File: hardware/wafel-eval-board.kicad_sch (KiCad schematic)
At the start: 50 parts, among them J101 CAN PORT, J102 SW, Q101 AO3422, U101 LM5163DDA

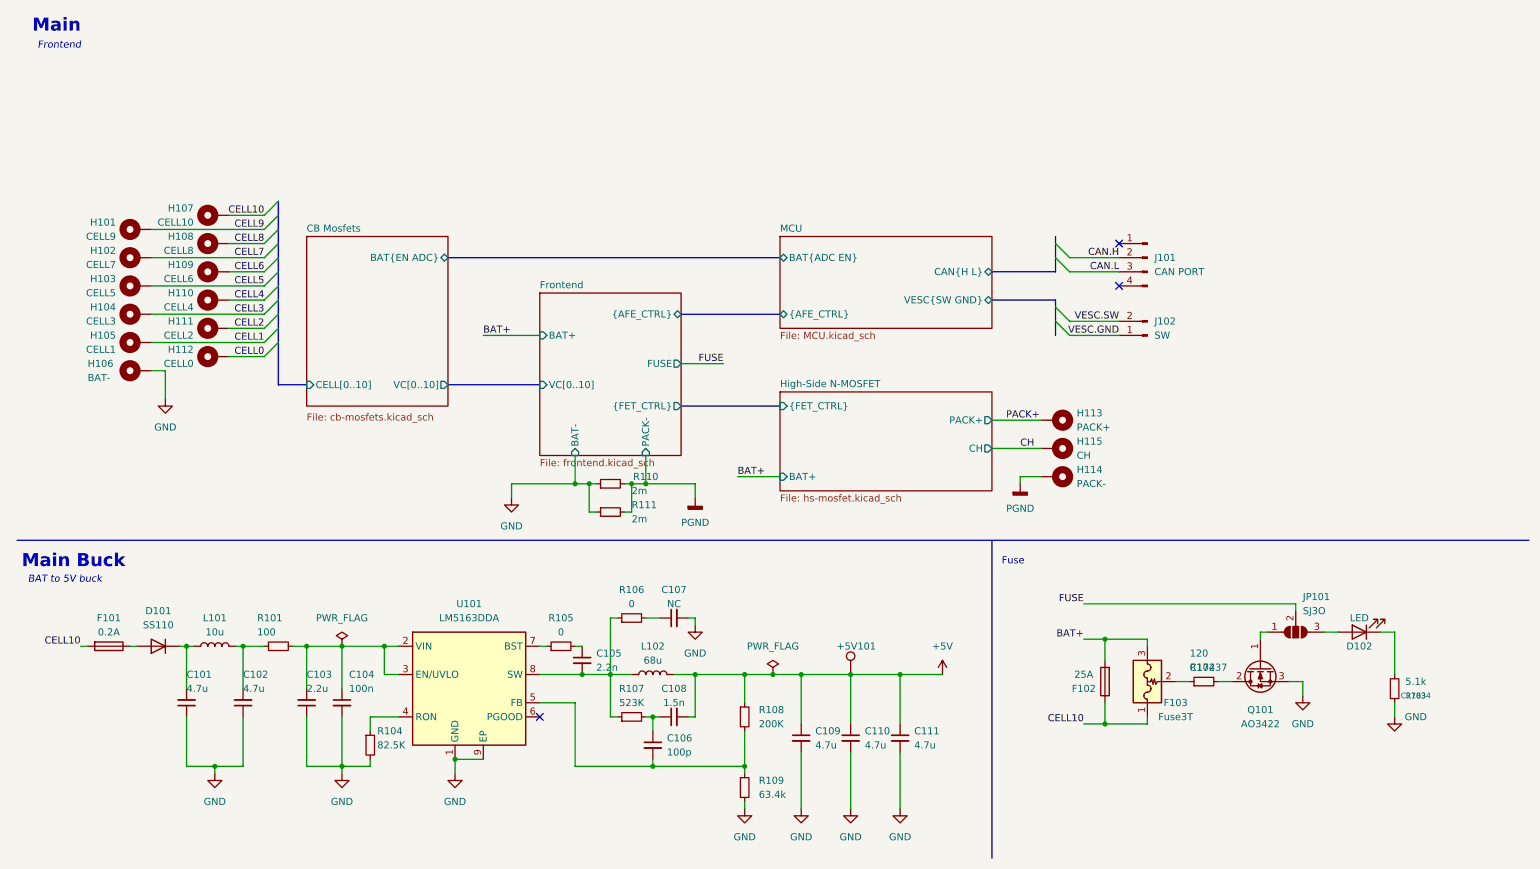
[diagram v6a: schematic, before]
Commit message: placed c mosfet
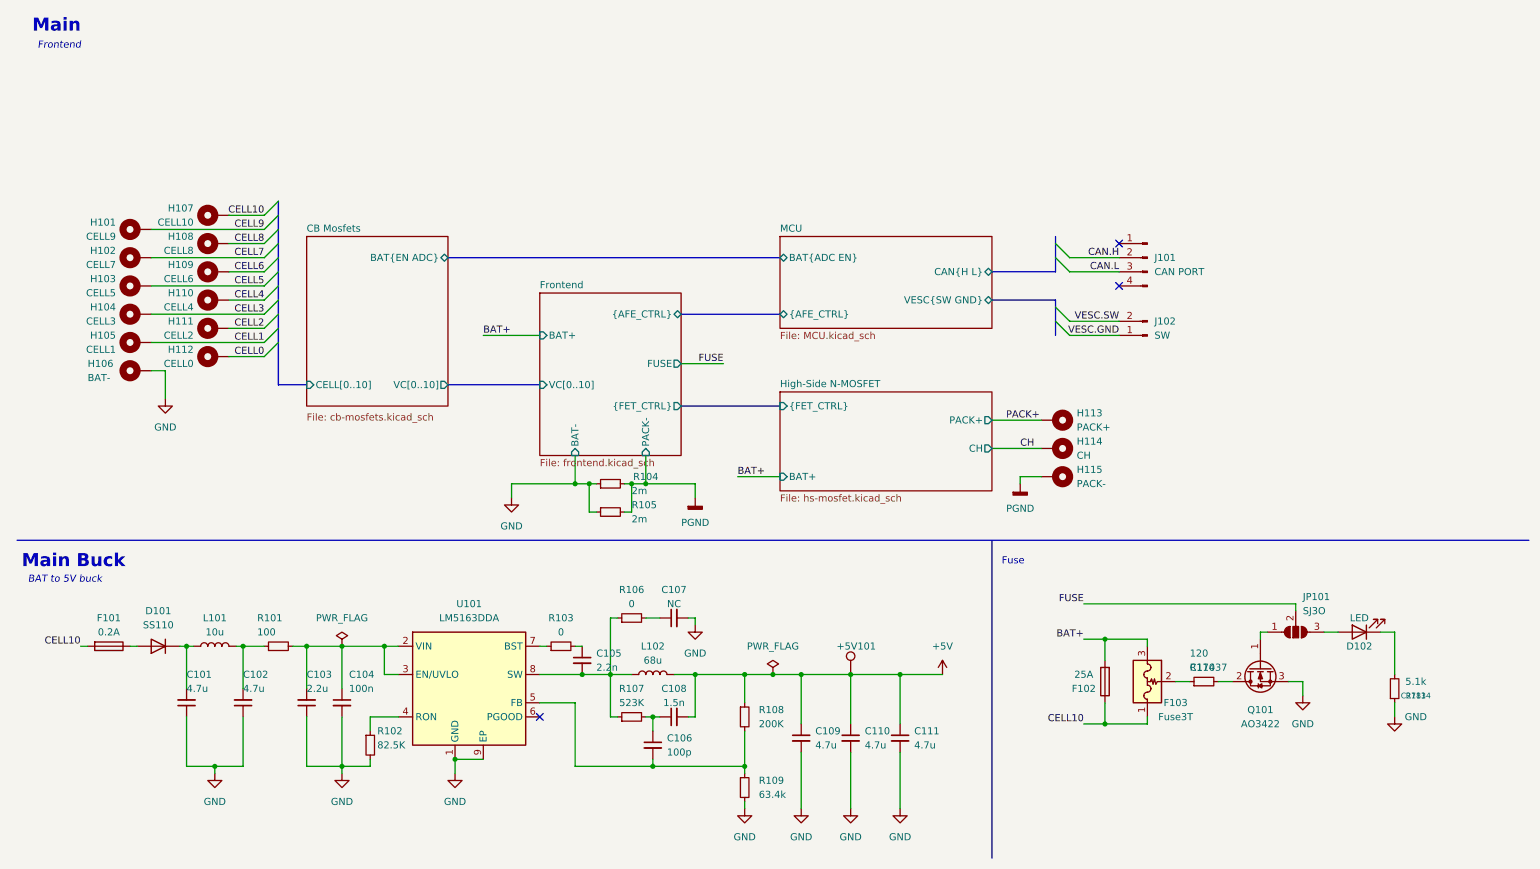
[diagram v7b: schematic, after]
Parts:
- C105, C106, C107, C108: footprint Capacitor_SMD:C_0805_2012Metric -> Capacitor_SMD:C_0603_1608Metric
- R101, R106, R107, R108, R109: footprint Resistor_SMD:R_0805_2012Metric -> Resistor_SMD:R_0603_1608Metric
- R102: renamed from R104; footprint Resistor_SMD:R_0805_2012Metric -> Resistor_SMD:R_0603_1608Metric
- R103: renamed from R105; footprint Resistor_SMD:R_0805_2012Metric -> Resistor_SMD:R_0603_1608Metric
- R104: renamed from R110; footprint Resistor_SMD:R_0805_2012Metric -> Resistor_SMD:R_0603_1608Metric
- R105: renamed from R111; footprint Resistor_SMD:R_0805_2012Metric -> Resistor_SMD:R_0603_1608Metric
- R110: renamed from R102; footprint Resistor_SMD:R_0805_2012Metric -> Resistor_SMD:R_0603_1608Metric
- R111: renamed from R103; footprint Resistor_SMD:R_0805_2012Metric -> Resistor_SMD:R_0603_1608Metric
- renumbered H115 to H114, H114 to H115
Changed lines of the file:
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@@
 		(in_pos_files yes)
 		(dnp no)
-		(property "Reference" "#PWR0105"
+		(property "Reference" "#PWR0115"
 			(at 260.35 147.32 0)
 			(hide yes)
@@
 			(project "wafel-eval-board"
 				(path "/3e668e3e-3e16-4665-a807-4735962c41d3"
-					(reference "#PWR0105")
+					(reference "#PWR0115")
 					(unit 1)
 				)
@@
 		(dnp no)
 		(fields_autoplaced yes)
-		(property "Reference" "#PWR0115"
+		(property "Reference" "#PWR0106"
 			(at 134.62 107.95 0)
 			(hide yes)
@@
 			(project "wafel-eval-board"
 				(path "/3e668e3e-3e16-4665-a807-4735962c41d3"
-					(reference "#PWR0115")
+					(reference "#PWR0106")
 					(unit 1)
 				)
@@
 		(dnp no)
 		(fields_autoplaced yes)
-		(property "Reference" "R105"
+		(property "Reference" "R103"
 			(at 110.49 123.19 90)
 			(show_name no)
@@
 			)
 		)
-		(property "Footprint" "Resistor_SMD:R_0805_2012Metric"
+		(property "Footprint" "Resistor_SMD:R_0603_1608Metric"
 			(at 110.49 128.27 0)
 			(hide yes)
@@
 			(project "wafel-eval-board"
 				(path "/3e668e3e-3e16-4665-a807-4735962c41d3"
-					(reference "R105")
+					(reference "R103")
 					(unit 1)
 				)
@@
 			)
 		)
-		(property "Footprint" "Capacitor_SMD:C_0805_2012Metric"
+		(property "Footprint" "Capacitor_SMD:C_0603_1608Metric"
 			(at 127 146.05 0)
 			(hide yes)
@@
 			)
 		)
-		(property "Footprint" "Resistor_SMD:R_0805_2012Metric"
+		(property "Footprint" "Resistor_SMD:R_0603_1608Metric"
 			(at 123.19 123.19 0)
 			(hide yes)
@@
 		(dnp no)
 		(fields_autoplaced yes)
-		(property "Reference" "#PWR0114"
+		(property "Reference" "#PWR0105"
 			(at 101.6 107.95 0)
 			(hide yes)
@@
 			(project "wafel-eval-board"
 				(path "/3e668e3e-3e16-4665-a807-4735962c41d3"
-					(reference "#PWR0114")
+					(reference "#PWR0105")
 					(unit 1)
 				)
@@
 			)
 		)
-		(property "Footprint" "Resistor_SMD:R_0805_2012Metric"
+		(property "Footprint" "Resistor_SMD:R_0603_1608Metric"
 			(at 143.51 140.97 0)
 			(hide yes)
@@
 			)
 		)
-		(property "Footprint" "Resistor_SMD:R_0805_2012Metric"
+		(property "Footprint" "Resistor_SMD:R_0603_1608Metric"
 			(at 123.19 140.97 0)
 			(hide yes)
@@
 		(dnp no)
 		(fields_autoplaced yes)
-		(property "Reference" "#FLG0102"
+		(property "Reference" "#FLG0101"
 			(at 71.12 126.365 0)
 			(hide yes)
@@
 			(project "wafel-eval-board"
 				(path "/3e668e3e-3e16-4665-a807-4735962c41d3"
-					(reference "#FLG0102")
+					(reference "#FLG0101")
 					(unit 1)
 				)
@@
 			)
 		)
-		(property "Footprint" "Resistor_SMD:R_0805_2012Metric"
+		(property "Footprint" "Resistor_SMD:R_0603_1608Metric"
 			(at 143.51 153.67 0)
 			(hide yes)
@@
 			)
 		)
-		(property "Footprint" "Capacitor_SMD:C_0805_2012Metric"
+		(property "Footprint" "Capacitor_SMD:C_0603_1608Metric"
 			(at 130.81 140.97 0)
 			(hide yes)
@@
 		(in_pos_files yes)
 		(dnp no)
-		(property "Reference" "R111"
+		(property "Reference" "R105"
 			(at 123.19 102.87 90)
 			(show_name no)
@@
 			)
 		)
-		(property "Footprint" "Resistor_SMD:R_0805_2012Metric"
+		(property "Footprint" "Resistor_SMD:R_0603_1608Metric"
 			(at 119.38 104.14 0)
 			(hide yes)
@@
 			(project "wafel-eval-board"
 				(path "/3e668e3e-3e16-4665-a807-4735962c41d3"
-					(reference "R111")
+					(reference "R105")
 					(unit 1)
 				)
@@
 		(dnp no)
 		(fields_autoplaced yes)
-		(property "Reference" "#PWR0104"
+		(property "Reference" "#PWR0103"
 			(at 71.12 157.48 0)
 			(hide yes)
@@
 			(project "wafel-eval-board"
 				(path "/3e668e3e-3e16-4665-a807-4735962c41d3"
-					(reference "#PWR0104")
+					(reference "#PWR0103")
 					(unit 1)
 				)
@@
 			)
 		)
-		(property "Footprint" "Capacitor_SMD:C_0805_2012Metric"
+		(property "Footprint" "Capacitor_SMD:C_0603_1608Metric"
 			(at 114.3 130.81 0)
 			(hide yes)
@@
 		(in_pos_files yes)
 		(dnp no)
-		(property "Reference" "R104"
+		(property "Reference" "R102"
 			(at 77.47 143.51 0)
 			(show_name no)
@@
 			)
 		)
-		(property "Footprint" "Resistor_SMD:R_0805_2012Metric"
+		(property "Footprint" "Resistor_SMD:R_0603_1608Metric"
 			(at 76.2 146.05 0)
 			(hide yes)
@@
 			(project "wafel-eval-board"
 				(path "/3e668e3e-3e16-4665-a807-4735962c41d3"
-					(reference "R104")
+					(reference "R102")
 					(unit 1)
 				)
@@
 		(in_pos_files yes)
 		(dnp no)
-		(property "Reference" "H114"
+		(property "Reference" "H115"
 			(at 203.2 96.5199 90)
 			(show_name no)
@@
 			(project "wafel-eval-board"
 				(path "/3e668e3e-3e16-4665-a807-4735962c41d3"
-					(reference "H114")
+					(reference "H115")
 					(unit 1)
 				)
@@
 			)
 		)
-		(property "Footprint" "Resistor_SMD:R_0805_2012Metric"
+		(property "Footprint" "Resistor_SMD:R_0603_1608Metric"
 			(at 59.69 128.27 0)
 			(hide yes)
@@
 		(in_pos_files yes)
 		(dnp no)
-		(property "Reference" "H115"
+		(property "Reference" "H114"
 			(at 203.2 91.4399 90)
 			(show_name no)
@@
 			(project "wafel-eval-board"
 				(path "/3e668e3e-3e16-4665-a807-4735962c41d3"
-					(reference "H115")
+					(reference "H114")
 					(unit 1)
 				)
@@
 		(in_pos_files yes)
 		(dnp no)
-		(property "Reference" "R110"
+		(property "Reference" "R104"
 			(at 125.73 97.79 90)
 			(show_name no)
@@
 			)
 		)
-		(property "Footprint" "Resistor_SMD:R_0805_2012Metric"
+		(property "Footprint" "Resistor_SMD:R_0603_1608Metric"
 			(at 119.38 99.06 0)
 			(hide yes)
@@
 			(project "wafel-eval-board"
 				(path "/3e668e3e-3e16-4665-a807-4735962c41d3"
-					(reference "R110")
+					(reference "R104")
 					(unit 1)
 				)
@@
 		(dnp no)
 		(fields_autoplaced yes)
-		(property "Reference" "#PWR0103"
+		(property "Reference" "#PWR0114"
 			(at 243.84 143.51 0)
 			(hide yes)
@@
 			(project "wafel-eval-board"
 				(path "/3e668e3e-3e16-4665-a807-4735962c41d3"
-					(reference "#PWR0103")
+					(reference "#PWR0114")
 					(unit 1)
 				)
@@
 		(in_pos_files yes)
 		(dnp no)
-		(property "Reference" "R103"
+		(property "Reference" "R111"
 			(at 264.16 137.16 0)
 			(show_name no)
@@
 			)
 		)
-		(property "Footprint" "Resistor_SMD:R_0805_2012Metric"
+		(property "Footprint" "Resistor_SMD:R_0603_1608Metric"
 			(at 260.35 135.89 0)
 			(hide yes)
@@
 			(project "wafel-eval-board"
 				(path "/3e668e3e-3e16-4665-a807-4735962c41d3"
-					(reference "R103")
+					(reference "R111")
 					(unit 1)
 				)
@@
 		(dnp no)
 		(fields_autoplaced yes)
-		(property "Reference" "#FLG0101"
+		(property "Reference" "#FLG0102"
 			(at 148.59 131.445 0)
 			(hide yes)
@@
 			(project "wafel-eval-board"
 				(path "/3e668e3e-3e16-4665-a807-4735962c41d3"
-					(reference "#FLG0101")
+					(reference "#FLG0102")
 					(unit 1)
 				)
@@
 			)
 		)
-		(property "Footprint" "Capacitor_SMD:C_0805_2012Metric"
+		(property "Footprint" "Capacitor_SMD:C_0603_1608Metric"
 			(at 130.81 123.19 0)
 			(hide yes)
@@
 		(in_pos_files yes)
 		(dnp no)
-		(property "Reference" "R102"
+		(property "Reference" "R110"
 			(at 223.52 132.08 90)
 			(show_name no)
@@
 			)
 		)
-		(property "Footprint" "Resistor_SMD:R_0805_2012Metric"
+		(property "Footprint" "Resistor_SMD:R_0603_1608Metric"
 			(at 226.06 134.62 0)
 			(hide yes)
@@
 			(project "wafel-eval-board"
 				(path "/3e668e3e-3e16-4665-a807-4735962c41d3"
-					(reference "R102")
+					(reference "R110")
 					(unit 1)
 				)
@@
 		(dnp no)
 		(fields_autoplaced yes)
-		(property "Reference" "#PWR0106"
+		(property "Reference" "#PWR0104"
 			(at 91.44 157.48 0)
 			(hide yes)
@@
 			(project "wafel-eval-board"
 				(path "/3e668e3e-3e16-4665-a807-4735962c41d3"
-					(reference "#PWR0106")
+					(reference "#PWR0104")
 					(unit 1)
 				)

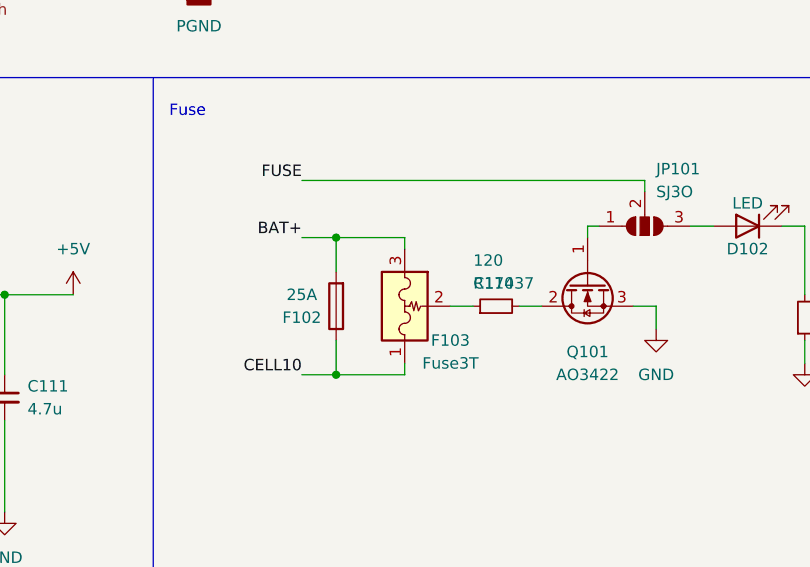
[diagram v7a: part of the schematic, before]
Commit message: placed c mosfet
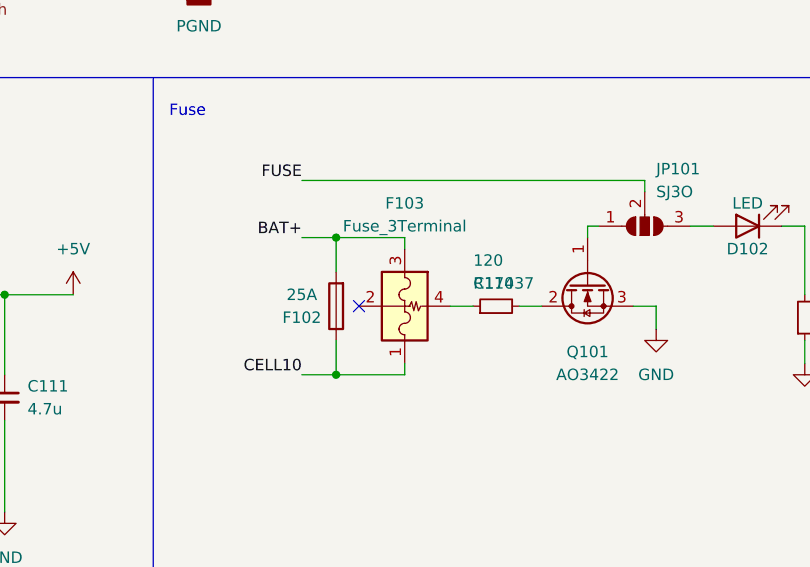
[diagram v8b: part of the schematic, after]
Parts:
- F103: value Fuse3T -> Fuse_3Terminal; footprint (none) -> wafel-eval-board:Fuse_SMD-3P_5.4x3.2mm
- JP101: footprint (none) -> Jumper:SolderJumper-3_P2.0mm_Open_TrianglePad1.0x1.5mm
- Q101: footprint (none) -> Package_TO_SOT_SMD:SOT-23
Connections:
- net at F103.2: no longer R110.1
- new net: F103.4, R110.1
- no-connect marks 3 -> 4
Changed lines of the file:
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@@
 	)
 	(no_connect
+		(at 210.82 134.62)
+	)
+	(no_connect
 		(at 210.82 63.5)
 	)
@@
 	)
 	(symbol
+		(lib_id "wafel-eval-board:Fuse_3Terminal")
+		(at 215.9 134.62 270)
+		(unit 1)
+		(body_style 1)
+		(exclude_from_sim no)
+		(in_bom yes)
+		(on_board yes)
+		(in_pos_files yes)
+		(dnp no)
+		(property "Reference" "F103"
+			(at 215.9 123.19 90)
+			(show_name no)
+			(do_not_autoplace no)
+			(effects
+				(font
+					(size 1.27 1.27)
+				)
+			)
+		)
+		(property "Value" "Fuse_3Terminal"
+			(at 215.9 125.73 90)
+			(show_name no)
+			(do_not_autoplace no)
+			(effects
+				(font
+					(size 1.27 1.27)
+				)
+			)
+		)
+		(property "Footprint" "wafel-eval-board:Fuse_SMD-3P_5.4x3.2mm"
+			(at 215.9 134.62 0)
+			(hide yes)
+			(show_name no)
+			(do_not_autoplace no)
+			(effects
+				(font
+					(size 1.27 1.27)
+				)
+			)
+		)
+		(property "Datasheet" ""
+			(at 215.9 134.62 0)
+			(hide yes)
+			(show_name no)
+			(do_not_autoplace no)
+			(effects
+				(font
+					(size 1.27 1.27)
+				)
+			)
+		)
+		(property "Description" "3-Terminal Battery Protection Fuse"
+			(at 215.9 134.62 0)
+			(hide yes)
+			(show_name no)
+			(do_not_autoplace no)
+			(effects
+				(font
+					(size 1.27 1.27)
+				)
+			)
+		)
+		(pin "3"
+		)
+		(pin "1"
+		)
+		(pin "4"
+		)
+		(pin "2"
+		)
+		(instances
+			(project "wafel-eval-board"
+				(path "/3e668e3e-3e16-4665-a807-4735962c41d3"
+					(reference "F103")
+					(unit 1)
+				)
+			)
+		)
+	)
+	(symbol
 		(lib_id "Mechanical:MountingHole_Pad")
 		(at 48.26 60.96 90)
@@
 			)
 		)
-		(property "Footprint" ""
+		(property "Footprint" "Package_TO_SOT_SMD:SOT-23"
 			(at 233.68 137.16 0)
 			(hide yes)
@@
 			)
 		)
-		(property "Footprint" ""
+		(property "Footprint" "Jumper:SolderJumper-3_P2.0mm_Open_TrianglePad1.0x1.5mm"
 			(at 242.57 125.73 0)
 			(hide yes)
@@
 					(unit 1)
 				)
-			)
-		)
-	)
-	(symbol
-		(lib_id "wafel-eval-board:Fuse_3Terminal")
-		(at 215.9 134.62 270)
-		(unit 1)
-		(body_style 1)
-		(exclude_from_sim no)
-		(in_bom yes)
-		(on_board yes)
-		(in_pos_files yes)
-		(dnp no)
-		(property "Reference" "F103"
-			(at 220.98 138.43 90)
-			(show_name no)
-			(do_not_autoplace no)
-			(effects
-				(font
-					(size 1.27 1.27)
-				)
-			)
-		)
-		(property "Value" "Fuse3T"
-			(at 220.98 140.97 90)
-			(show_name no)
-			(do_not_autoplace no)
-			(effects
-				(font
-					(size 1.27 1.27)
-				)
-			)
-		)
-		(property "Footprint" ""
-			(at 215.9 134.62 0)
-			(hide yes)
-			(show_name no)
-			(do_not_autoplace no)
-			(effects
-				(font
-					(size 1.27 1.27)
-				)
-			)
-		)
-		(property "Datasheet" ""
-			(at 215.9 134.62 0)
-			(hide yes)
-			(show_name no)
-			(do_not_autoplace no)
-			(effects
-				(font
-					(size 1.27 1.27)
-				)
-			)
-		)
-		(property "Description" "3-Terminal Battery Protection Fuse"
-			(at 215.9 134.62 0)
-			(hide yes)
-			(show_name no)
-			(do_not_autoplace no)
-			(effects
-				(font
-					(size 1.27 1.27)
-				)
-			)
-		)
-		(pin "1"
-		)
-		(pin "2"
-		)
-		(pin "3"
-		)
-		(instances
-			(project "wafel-eval-board"
-				(path "/3e668e3e-3e16-4665-a807-4735962c41d3"
-					(reference "F103")
-					(unit 1)
-				)
